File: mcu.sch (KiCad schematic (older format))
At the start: 24 parts, among them J1 USB_C_Receptacle_USB2.0, U1 STM32F103C8Tx, U2 XC6206PxxxMR, U3 SRV05-4, Y1 8MHz

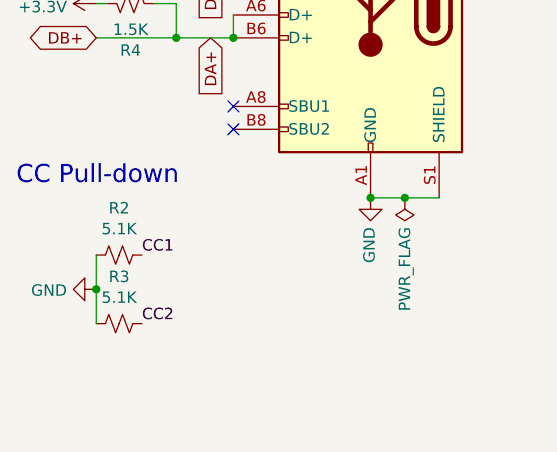
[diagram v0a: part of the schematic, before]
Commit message: Floated the shield
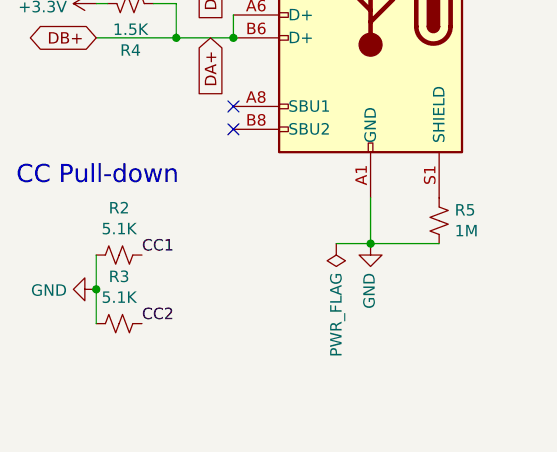
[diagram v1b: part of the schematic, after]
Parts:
- added R5: 1M, Resistor_SMD:R_0402_1005Metric, symbol Device:R_Small_US
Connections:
- net GND: now also R5.1; no longer J1.S1 (SHIELD)
- new net: J1.S1 (SHIELD), R5.2
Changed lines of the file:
@@
-$EndComp
-$Comp
-L power:GND #PWR026
-U 1 1 5E98E0EB
-P 10200 5700
-F 0 "#PWR026" H 10200 5450 50  0001 C CNN
-F 1 "GND" V 10205 5572 50  0000 R CNN
-F 2 "" H 10200 5700 50  0001 C CNN
-F 3 "" H 10200 5700 50  0001 C CNN
-	1    10200 5700
-	-1   0    0    -1
 $EndComp
 $Comp
@@
 L power:PWR_FLAG #FLG02
 U 1 1 5E98E148
-P 10350 5700
-F 0 "#FLG02" H 10350 5775 50  0001 C CNN
-F 1 "PWR_FLAG" V 10350 5827 50  0000 L CNN
-F 2 "" H 10350 5700 50  0001 C CNN
-F 3 "~" H 10350 5700 50  0001 C CNN
-	1    10350 5700
+P 10050 5900
+F 0 "#FLG02" H 10050 5975 50  0001 C CNN
+F 1 "PWR_FLAG" V 10050 6027 50  0000 L CNN
+F 2 "" H 10050 5900 50  0001 C CNN
+F 3 "~" H 10050 5900 50  0001 C CNN
+	1    10050 5900
 	-1   0    0    1
 $EndComp
@@
 	-1   0    0    -1
 $EndComp
-Wire Wire Line
-	10200 5700 10350 5700
-Connection ~ 10200 5700
-Connection ~ 10350 5700
-Wire Wire Line
-	10350 5700 10500 5700
 NoConn ~ 9600 5300
 NoConn ~ 9600 5400
@@
 	0    1    1    0
 $EndComp
+$Comp
+L power:GND #PWR026
+U 1 1 5E98E0EB
+P 10200 5900
+F 0 "#PWR026" H 10200 5650 50  0001 C CNN
+F 1 "GND" V 10205 5772 50  0000 R CNN
+F 2 "" H 10200 5900 50  0001 C CNN
+F 3 "" H 10200 5900 50  0001 C CNN
+	1    10200 5900
+	-1   0    0    -1
+$EndComp
+$Comp
+L Device:R_Small_US R5
+U 1 1 5EAEDAFD
+P 10500 5800
+F 0 "R5" H 10432 5754 50  0000 R CNN
+F 1 "1M" H 10432 5845 50  0000 R CNN
+F 2 "Resistor_SMD:R_0402_1005Metric" H 10500 5800 50  0001 C CNN
+F 3 "~" H 10500 5800 50  0001 C CNN
+F 4 "C26083" H 10500 5800 50  0001 C CNN "LCSC"
+	1    10500 5800
+	-1   0    0    1
+$EndComp
+Wire Wire Line
+	10200 5900 10050 5900
+Wire Wire Line
+	10200 5700 10200 5900
+Connection ~ 10200 5900
+Wire Wire Line
+	10200 5900 10500 5900
 $EndSCHEMATC
